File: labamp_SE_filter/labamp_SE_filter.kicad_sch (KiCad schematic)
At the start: 13 parts, among them J1 Conn_02x06_Odd_Even, J2 Conn_02x06_Odd_Even, J3 Conn_01x03

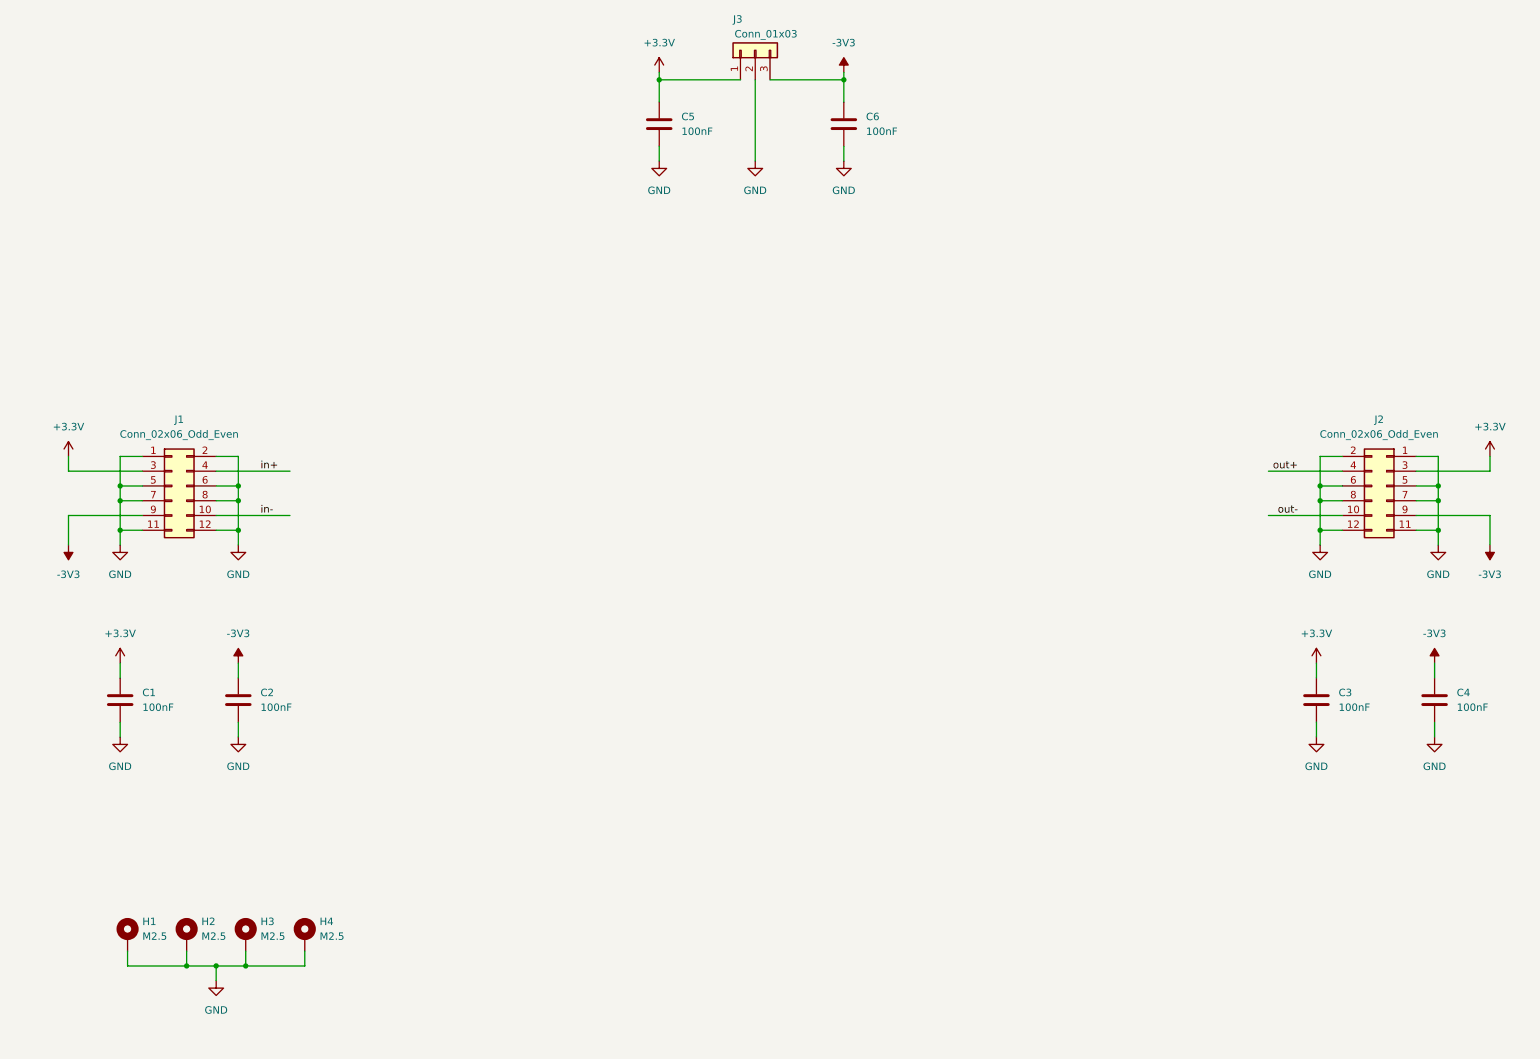
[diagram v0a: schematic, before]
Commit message: Updated SE filter schematics
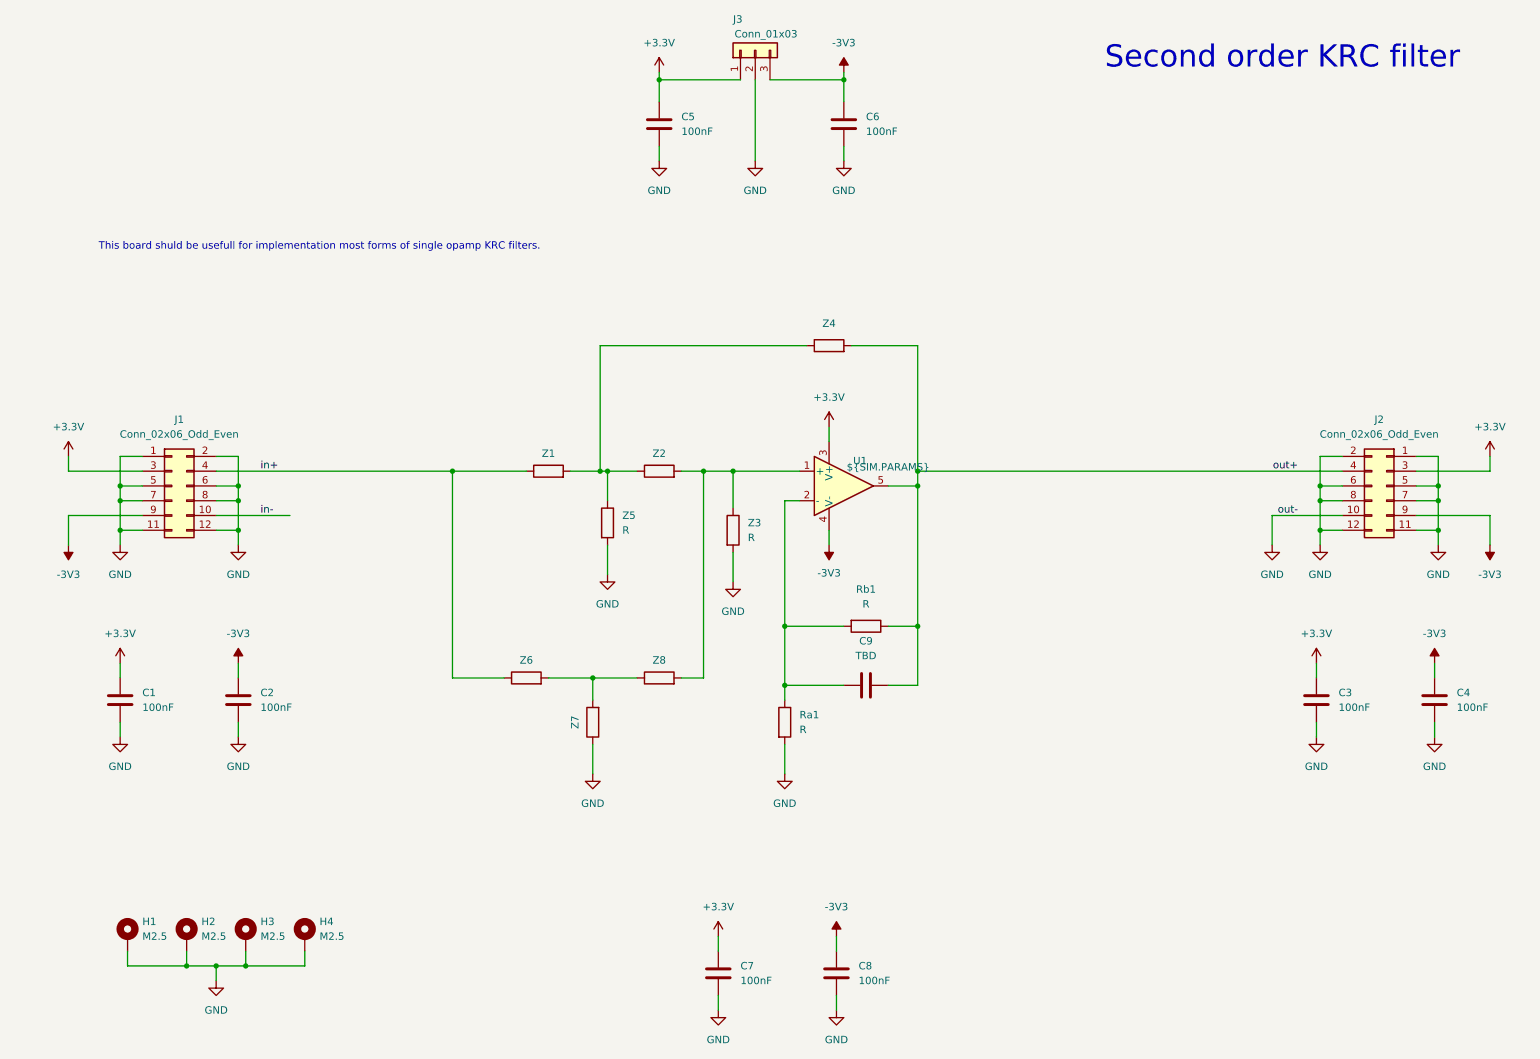
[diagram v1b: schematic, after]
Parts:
- added C7, C8: 100nF, Capacitor_SMD:C_0603_1608Metric_Pad1.08x0.95mm_HandSolder, symbol Device:C
- added C9: TBD, Capacitor_SMD:C_0603_1608Metric_Pad1.08x0.95mm_HandSolder, symbol Device:C
- added Ra1, Rb1, Z1, Z2, Z3, Z4, Z5, Z6, Z7, Z8: R, Resistor_SMD:R_0603_1608Metric_Pad0.98x0.95mm_HandSolder, symbol Device:R
- added U1: ${SIM.PARAMS}, SOT-23-5, symbol Simulation_SPICE:OPAMP
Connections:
- net out- is gone; now on net GND: J2.10 (Pin_10)
- net +3.3V: now also C7.1, U1.3 (V+)
- net -3V3: now also C8.1, U1.4 (V-)
- net GND: now also C7.2, C8.2, Ra1.2, Z3.2, Z5.2, Z7.1
- net in+: now also Z1.1, Z6.1
- net out+: now also C9.2, Rb1.1, U1.5, Z4.2
- new net: Z1.2, Z2.1, Z4.1, Z5.1
- new net: Z6.2, Z7.2, Z8.1
- new net: U1.1 (+), Z2.2, Z3.1, Z8.2
- new net: C9.1, Ra1.1, Rb1.2, U1.2 (-)
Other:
- note added: "Second order KRC filter"
- note added: "This board shuld be usefull for implementation most forms of single opamp KRC filters."

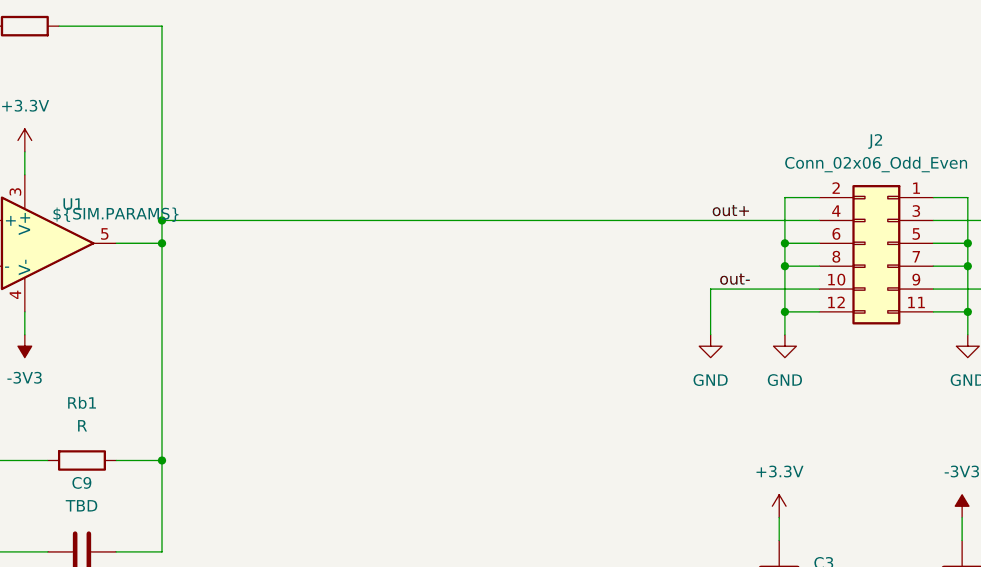
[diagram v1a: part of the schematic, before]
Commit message: Added output resistors to Single ended filter schematics
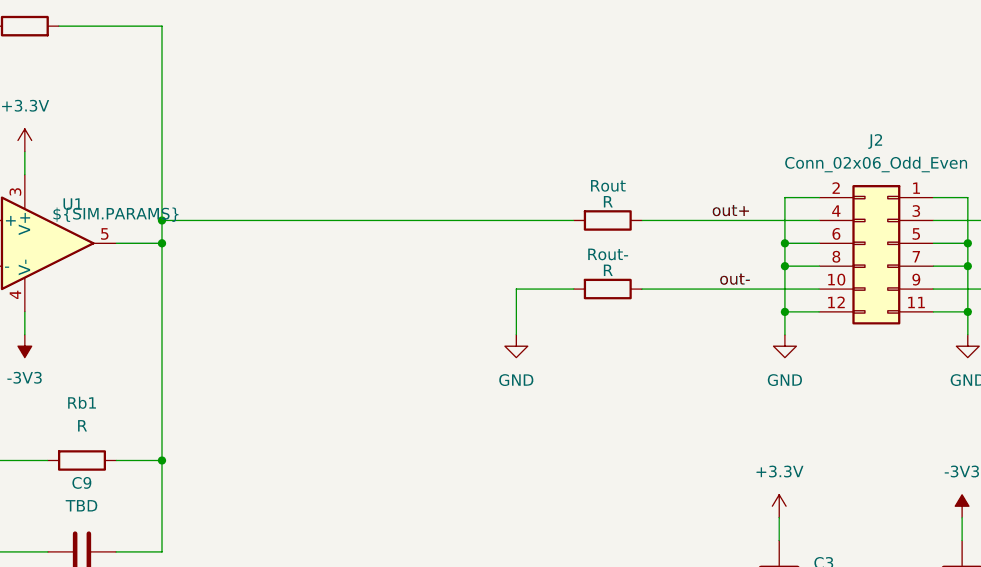
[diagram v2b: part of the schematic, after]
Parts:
- added Rout, Rout-: R, Resistor_SMD:R_0603_1608Metric_Pad0.98x0.95mm_HandSolder, symbol Device:R
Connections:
- net GND: now also Rout-.2; no longer J2.10 (Pin_10)
- net out+: now also Rout.1; no longer C9.2, Rb1.1, U1.5, Z4.2
- new net: C9.2, Rb1.1, Rout.2, U1.5, Z4.2
- new net out-: J2.10 (Pin_10), Rout-.1
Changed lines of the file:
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@@
 	(wire
 		(pts
+			(xy 217.17 99.06) (xy 210.82 99.06)
+		)
+		(stroke
+			(width 0)
+			(type default)
+		)
+	)
+	(wire
+		(pts
 			(xy 148.59 96.52) (xy 151.13 96.52)
 		)
@@
 	(wire
 		(pts
+			(xy 224.79 91.44) (xy 244.475 91.44)
+		)
+		(stroke
+			(width 0)
+			(type default)
+		)
+	)
+	(wire
+		(pts
 			(xy 260.35 134.62) (xy 260.35 137.16)
 		)
@@
 	(wire
 		(pts
-			(xy 244.475 99.06) (xy 232.41 99.06)
+			(xy 244.475 99.06) (xy 224.79 99.06)
 		)
 		(stroke
@@
 	(wire
 		(pts
-			(xy 171.45 91.44) (xy 244.475 91.44)
+			(xy 171.45 91.44) (xy 217.17 91.44)
 		)
 		(stroke
@@
 	(wire
 		(pts
-			(xy 232.41 99.06) (xy 232.41 104.14)
+			(xy 210.82 99.06) (xy 210.82 104.14)
 		)
 		(stroke
@@
 	(symbol
 		(lib_id "Device:R")
+		(at 220.98 91.44 270)
+		(unit 1)
+		(exclude_from_sim no)
+		(in_bom yes)
+		(on_board yes)
+		(dnp no)
+		(property "Reference" "Rout"
+			(at 220.98 87.63 90)
+			(effects
+				(font
+					(size 1.27 1.27)
+				)
+			)
+		)
+		(property "Value" "R"
+			(at 220.98 89.408 90)
+			(effects
+				(font
+					(size 1.27 1.27)
+				)
+			)
+		)
+		(property "Footprint" "Resistor_SMD:R_0603_1608Metric_Pad0.98x0.95mm_HandSolder"
+			(at 220.98 89.662 90)
+			(effects
+				(font
+					(size 1.27 1.27)
+				)
+				(hide yes)
+			)
+		)
+		(property "Datasheet" "~"
+			(at 220.98 91.44 0)
+			(effects
+				(font
+					(size 1.27 1.27)
+				)
+				(hide yes)
+			)
+		)
+		(property "Description" "Resistor"
+			(at 220.98 91.44 0)
+			(effects
+				(font
+					(size 1.27 1.27)
+				)
+				(hide yes)
+			)
+		)
+		(pin "2"
+		)
+		(pin "1"
+		)
+		(instances
+			(project "labamp_SE_filter"
+				(path "/a0c99055-08c7-4e05-9803-96c7ce32a2b2"
+					(reference "Rout")
+					(unit 1)
+				)
+			)
+		)
+	)
+	(symbol
+		(lib_id "Device:R")
 		(at 156.21 69.85 90)
 		(unit 1)
@@
 	)
 	(symbol
+		(lib_id "Device:R")
+		(at 220.98 99.06 270)
+		(unit 1)
+		(exclude_from_sim no)
+		(in_bom yes)
+		(on_board yes)
+		(dnp no)
+		(property "Reference" "Rout-"
+			(at 220.98 95.25 90)
+			(effects
+				(font
+					(size 1.27 1.27)
+				)
+			)
+		)
+		(property "Value" "R"
+			(at 220.98 97.028 90)
+			(effects
+				(font
+					(size 1.27 1.27)
+				)
+			)
+		)
+		(property "Footprint" "Resistor_SMD:R_0603_1608Metric_Pad0.98x0.95mm_HandSolder"
+			(at 220.98 97.282 90)
+			(effects
+				(font
+					(size 1.27 1.27)
+				)
+				(hide yes)
+			)
+		)
+		(property "Datasheet" "~"
+			(at 220.98 99.06 0)
+			(effects
+				(font
+					(size 1.27 1.27)
+				)
+				(hide yes)
+			)
+		)
+		(property "Description" "Resistor"
+			(at 220.98 99.06 0)
+			(effects
+				(font
+					(size 1.27 1.27)
+				)
+				(hide yes)
+			)
+		)
+		(pin "2"
+		)
+		(pin "1"
+		)
+		(instances
+			(project "labamp_SE_filter"
+				(path "/a0c99055-08c7-4e05-9803-96c7ce32a2b2"
+					(reference "Rout-")
+					(unit 1)
+				)
+			)
+		)
+	)
+	(symbol
 		(lib_id "power:-3V3")
 		(at 25.4 104.14 180)
@@
 	(symbol
 		(lib_id "power:GND")
-		(at 232.41 104.14 0)
+		(at 210.82 104.14 0)
 		(mirror y)
 		(unit 1)
@@
 		(fields_autoplaced yes)
 		(property "Reference" "#PWR031"
-			(at 232.41 110.49 0)
+			(at 210.82 110.49 0)
 			(effects
 				(font
@@
 		)
 		(property "Value" "GND"
-			(at 232.41 109.22 0)
+			(at 210.82 109.22 0)
 			(effects
 				(font
@@
 		)
 		(property "Footprint" ""
-			(at 232.41 104.14 0)
+			(at 210.82 104.14 0)
 			(effects
 				(font
@@
 		)
 		(property "Datasheet" ""
-			(at 232.41 104.14 0)
+			(at 210.82 104.14 0)
 			(effects
 				(font
@@
 		)
 		(property "Description" "Power symbol creates a global label with name \"GND\" , ground"
-			(at 232.41 104.14 0)
+			(at 210.82 104.14 0)
 			(effects
 				(font
